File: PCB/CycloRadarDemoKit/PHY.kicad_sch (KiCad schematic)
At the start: 34 parts, among them J201 ARJM11B1-009-AB-EW2, U201 IP101GRI, Y201 25MHz

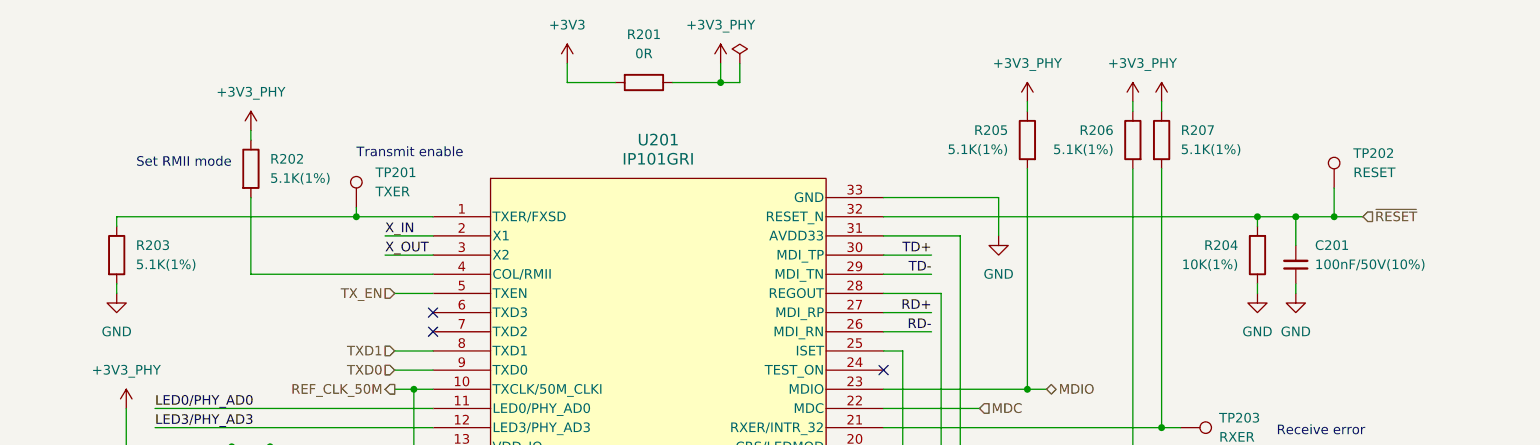
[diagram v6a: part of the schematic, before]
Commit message: Schematic edited, split sheets
improved PM diagram
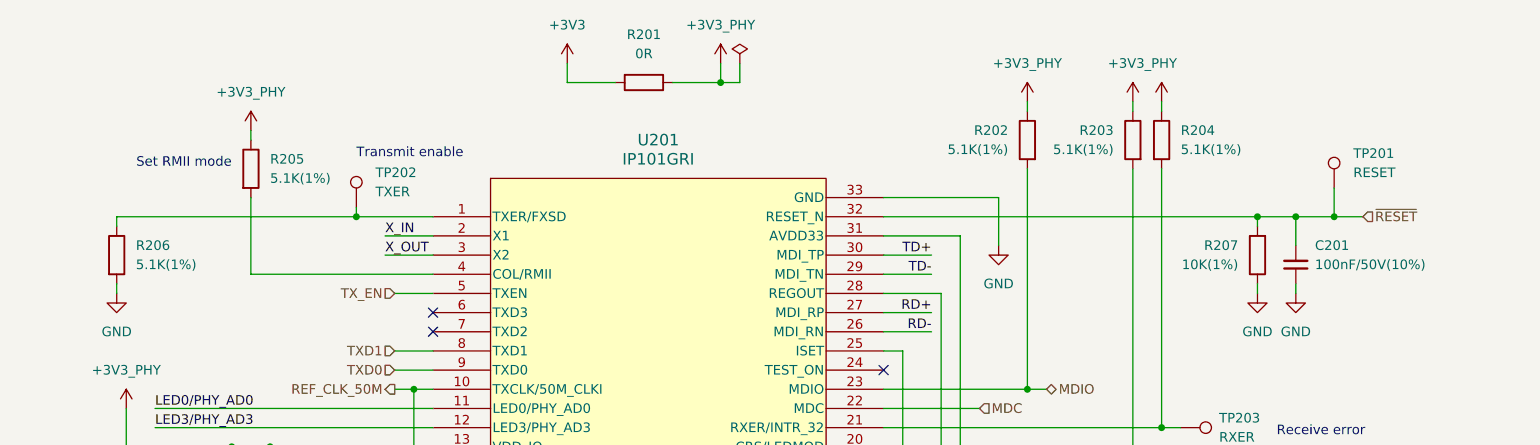
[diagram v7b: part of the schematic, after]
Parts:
- renumbered R205 to R202, R206 to R203, R207 to R204, R202 to R205, R203 to R206, R204 to R207, TP202 to TP201, TP201 to TP202

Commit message: starting the mockup
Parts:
- J201: footprint Connector_RJ:RJ45_Abracon_ARJM11B1-009-AB-EW2_ABR -> Connector_RJ:RJ45_OST_PJ012-8P8CX_Vertical; Note (none) -> Wrong footprint
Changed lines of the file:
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@@
       (effects (font (size 1.27 1.27)))
     )
-    (property "Footprint" "Connector_RJ:RJ45_Abracon_ARJM11B1-009-AB-EW2_ABR" (at 71.12 130.81 0)
+    (property "Footprint" "Connector_RJ:RJ45_OST_PJ012-8P8CX_Vertical" (at 71.12 130.81 0)
       (effects (font (size 1.27 1.27)) hide)
     )
@@
       (effects (font (size 1.27 1.27)) hide)
     )
+    (property "Note" "Wrong footprint" (at 71.12 143.51 0)
+      (effects (font (size 1.27 1.27)) hide)
+    )
